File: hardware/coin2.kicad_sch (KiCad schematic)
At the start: 27 parts, among them J1 Conn_01x04, J2 Conn_01x03, U1 WCH CH32V003F4U6

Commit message: cleanup some hole locations etc.
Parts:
- J1, J2: now fitted
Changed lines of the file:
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@@
 		(in_bom no)
 		(on_board yes)
-		(dnp yes)
+		(dnp no)
 		(property "Reference" "J1"
 			(at 52.07 86.36 0)
@@
 		(in_bom no)
 		(on_board yes)
-		(dnp yes)
+		(dnp no)
 		(fields_autoplaced yes)
 		(property "Reference" "J2"

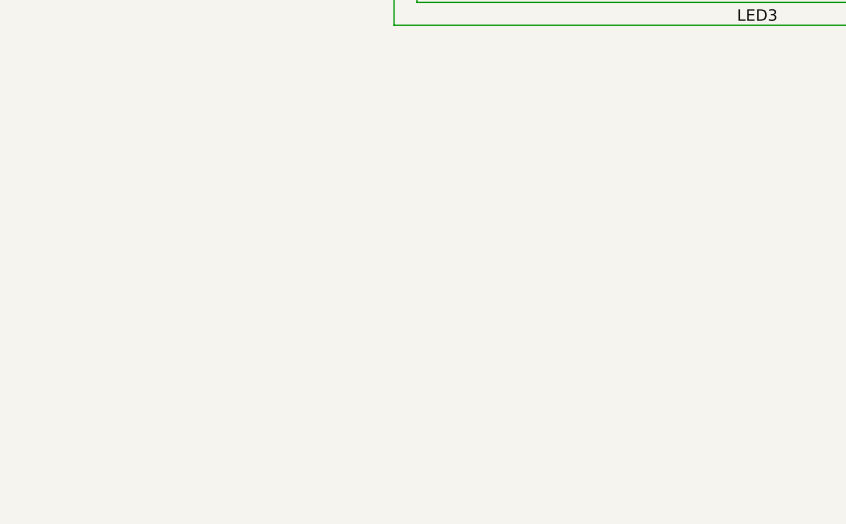
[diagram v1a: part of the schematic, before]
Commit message: add bypass caps, tweak clearance holes
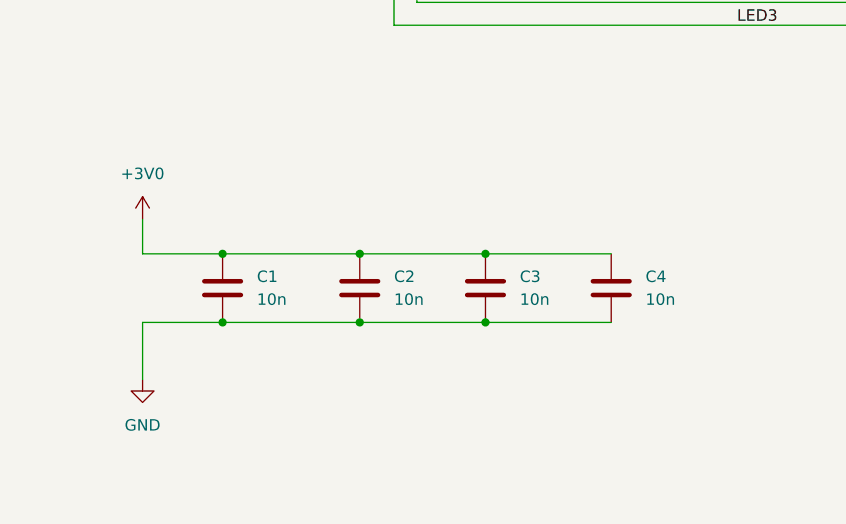
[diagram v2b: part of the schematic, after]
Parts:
- added C1, C2, C3, C4: 10n, Capacitor_SMD:C_0402_1005Metric, symbol Device:C
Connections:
- net +3V0: now also C1.1, C2.1, C3.1, C4.1
- net GND: now also C1.2, C2.2, C3.2, C4.2

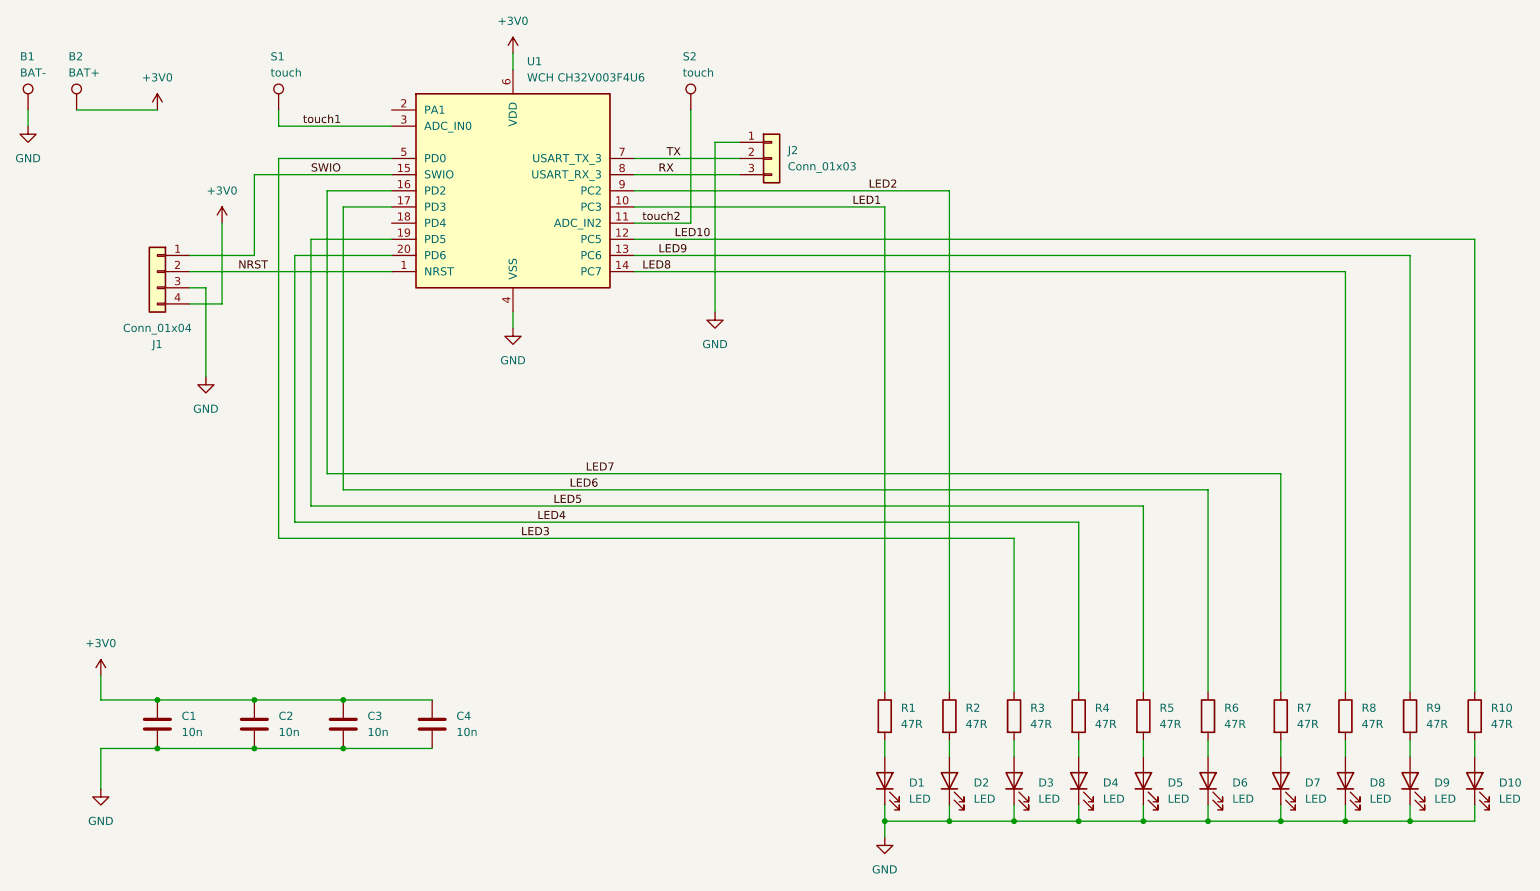
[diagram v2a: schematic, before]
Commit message: change connectors from 2.54 to 1.27mm spacing, add decoupling
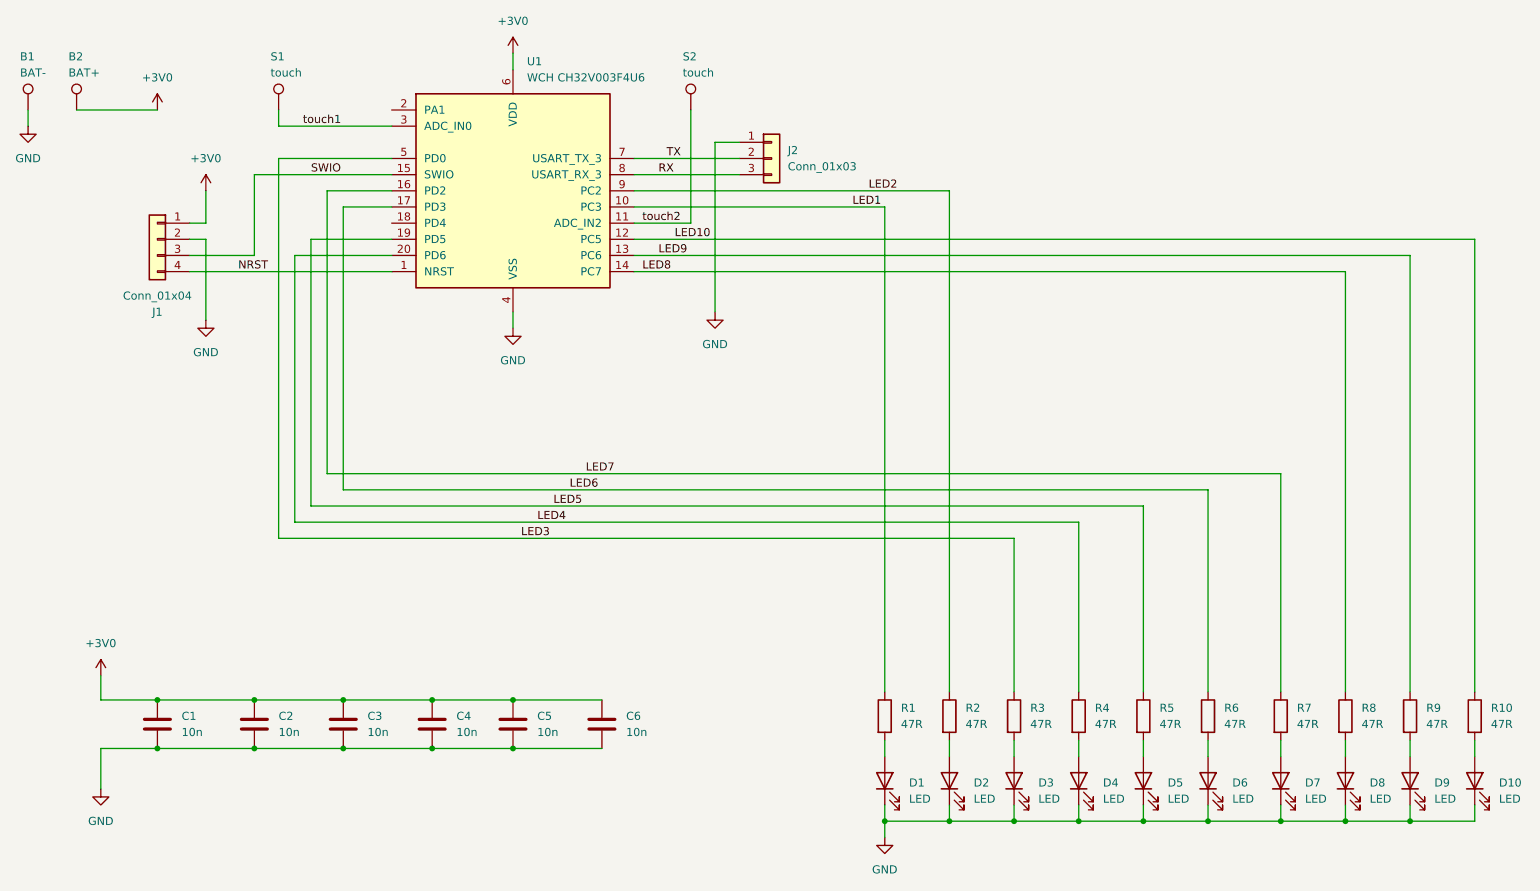
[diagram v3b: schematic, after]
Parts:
- added C5, C6: 10n, Capacitor_SMD:C_0402_1005Metric, symbol Device:C
- J1: footprint Connector_PinHeader_2.54mm:PinHeader_1x04_P2.54mm_Vertical -> Connector_PinHeader_1.27mm:PinHeader_1x04_P1.27mm_Vertical
- J2: footprint Connector_PinHeader_2.54mm:PinHeader_1x03_P2.54mm_Vertical -> Connector_PinHeader_1.27mm:PinHeader_1x03_P1.27mm_Vertical
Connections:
- net +3V0: now also J1.1 (Pin_1), C5.1, C6.1; no longer J1.4 (Pin_4)
- net GND: now also J1.2 (Pin_2), C5.2, C6.2; no longer J1.3 (Pin_3)
- net NRST: now also J1.4 (Pin_4); no longer J1.2 (Pin_2)
- net SWIO: now also J1.3 (Pin_3); no longer J1.1 (Pin_1)
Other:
- moved on the sheet: J1
